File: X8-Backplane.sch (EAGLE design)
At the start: 3 parts

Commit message: Fleshing out the idea for the backplane
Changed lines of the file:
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@@
 <part name="FRAME1" library="frames" deviceset="A4-SMALL-DOCFIELD" device=""/>
 <part name="U$1" library="HSEC8-1xx-01-XX-DV-A" deviceset="HSEC8-140-01-XX-DV-A" device=""/>
+<part name="U$17" library="HSEC8-1xx-01-XX-DV-A" deviceset="HSEC8-140-01-XX-DV-A" device=""/>
 <part name="U$2" library="HSEC8-1xx-01-XX-DV-A" deviceset="HSEC8-160-01-XX-DV-A" device=""/>
-<part name="U$17" library="HSEC8-1xx-01-XX-DV-A" deviceset="HSEC8-140-01-XX-DV-A" device=""/>
 </parts>
 <sheets>
@@
 <instance part="FRAME1" gate="/1" x="0" y="0"/>
 <instance part="U$1" gate="G$1" x="50.8" y="190.5"/>
-<instance part="U$2" gate="G$1" x="114.3" y="220.98"/>
 <instance part="U$17" gate="G$1" x="15.24" y="190.5"/>
+<instance part="U$2" gate="G$1" x="91.44" y="185.42"/>
 </instances>
 <busses>

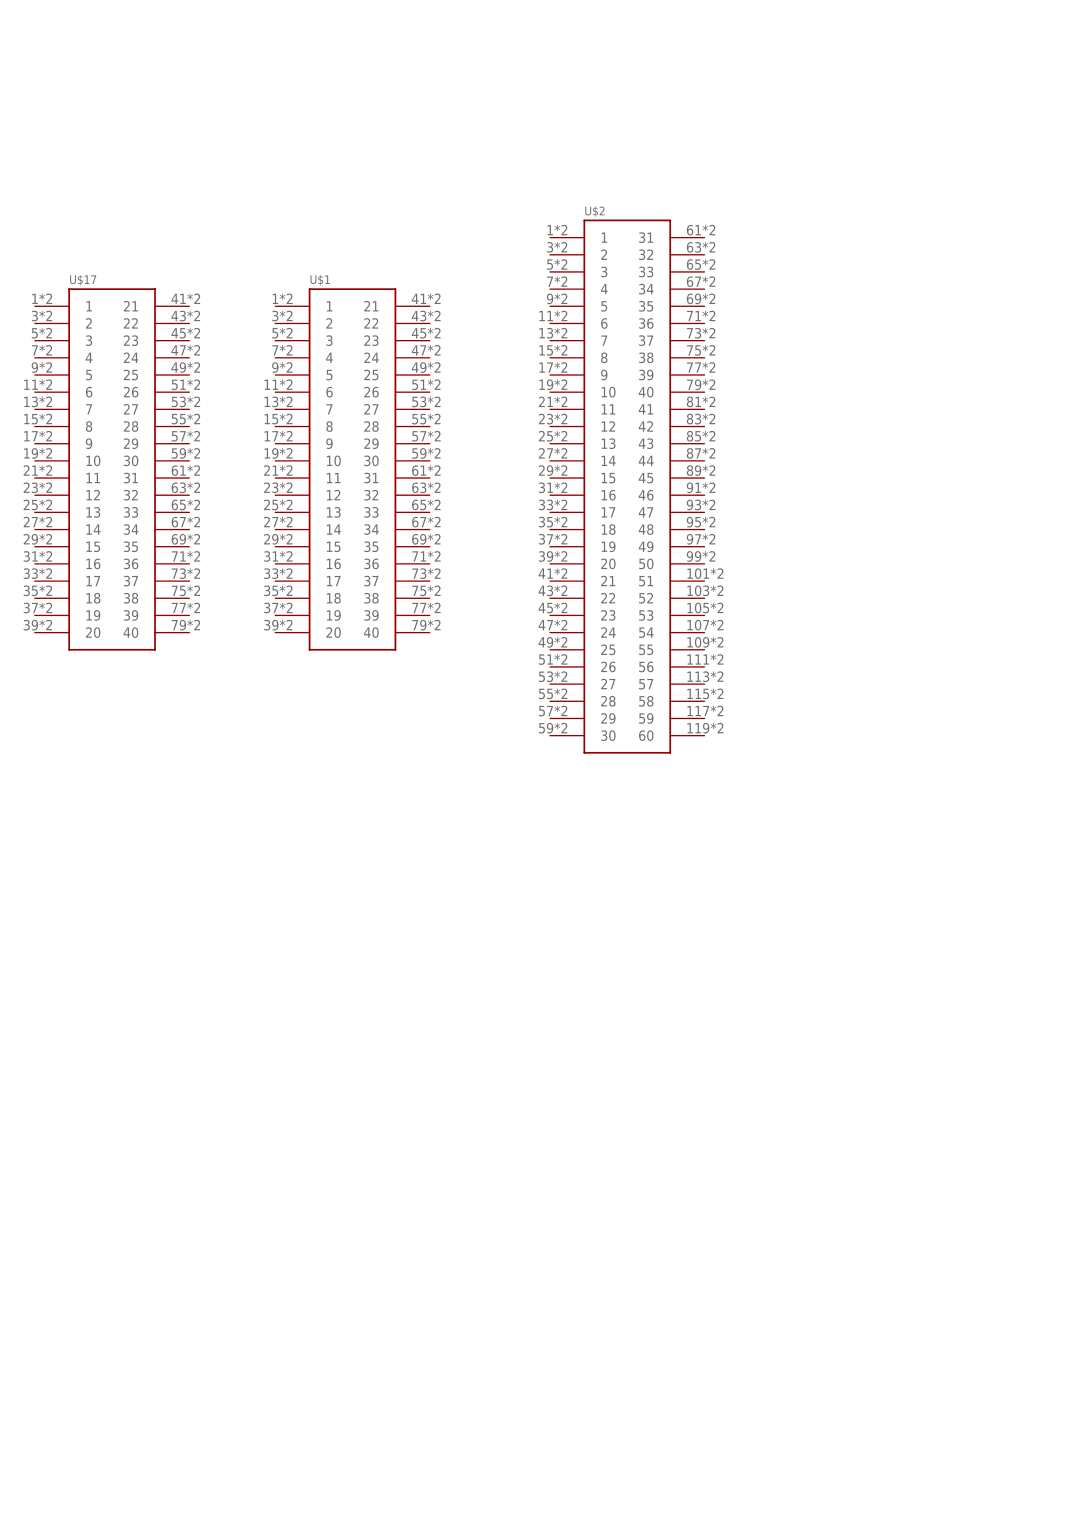
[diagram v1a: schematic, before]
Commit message: Added more connections to the backplane
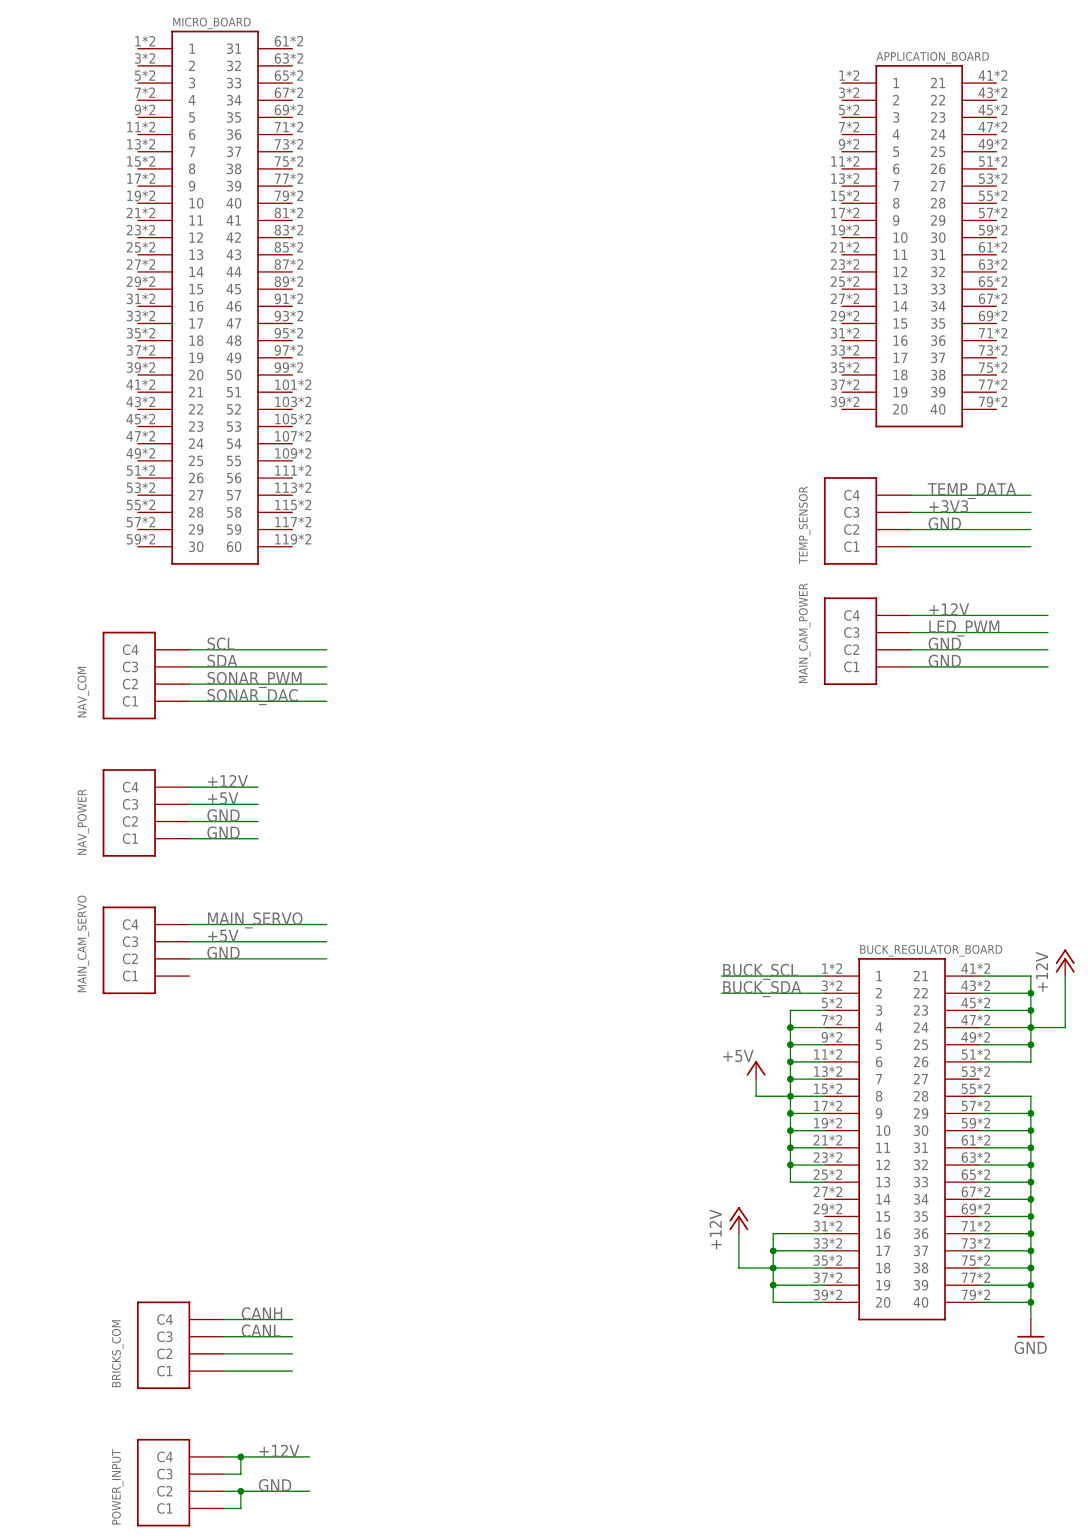
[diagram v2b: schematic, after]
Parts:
- removed U$1, U$17: HSEC8-140-01-XX-DV-A, HSEC8-1xx-01-XX-DV-A:HSEC8-140-01-XX-DV-A
- removed U$2: HSEC8-160-01-XX-DV-A, HSEC8-1xx-01-XX-DV-A:HSEC8-160-01-XX-DV-A
- added APPLICATION_BOARD, BUCK_REGULATOR_BOARD: HSEC8-140-01-XX-DV-A, HSEC8-1xx-01-XX-DV-A:HSEC8-140-01-XX-DV-A
- added BRICKS_COM, MAIN_CAM_POWER, MAIN_CAM_SERVO, NAV_COM, NAV_POWER, POWER_INPUT, TEMP_SENSOR: MICRO-FIT-4-SMD-PART, Connectors:MICRO-FIT-4-SMD-PART
- added MICRO_BOARD: HSEC8-160-01-XX-DV-A, HSEC8-1xx-01-XX-DV-A:HSEC8-160-01-XX-DV-A
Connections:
- new net +12V: BUCK_REGULATOR_BOARD.16, BUCK_REGULATOR_BOARD.17, BUCK_REGULATOR_BOARD.18, BUCK_REGULATOR_BOARD.19, BUCK_REGULATOR_BOARD.20, BUCK_REGULATOR_BOARD.21, BUCK_REGULATOR_BOARD.22, BUCK_REGULATOR_BOARD.23, BUCK_REGULATOR_BOARD.24, BUCK_REGULATOR_BOARD.25, BUCK_REGULATOR_BOARD.26, MAIN_CAM_POWER.C4, NAV_POWER.C4, POWER_INPUT.C3, POWER_INPUT.C4
- new net +3V3: TEMP_SENSOR.C3
- new net +5V: BUCK_REGULATOR_BOARD.10, BUCK_REGULATOR_BOARD.11, BUCK_REGULATOR_BOARD.12, BUCK_REGULATOR_BOARD.13, BUCK_REGULATOR_BOARD.3, BUCK_REGULATOR_BOARD.4, BUCK_REGULATOR_BOARD.5, BUCK_REGULATOR_BOARD.6, BUCK_REGULATOR_BOARD.7, BUCK_REGULATOR_BOARD.8, BUCK_REGULATOR_BOARD.9, MAIN_CAM_SERVO.C3, NAV_POWER.C3
- new net BUCK_SCL: BUCK_REGULATOR_BOARD.1
- new net BUCK_SDA: BUCK_REGULATOR_BOARD.2
- new net CANH: BRICKS_COM.C4
- new net CANL: BRICKS_COM.C3
- new net GND: BUCK_REGULATOR_BOARD.28, BUCK_REGULATOR_BOARD.29, BUCK_REGULATOR_BOARD.30, BUCK_REGULATOR_BOARD.31, BUCK_REGULATOR_BOARD.32, BUCK_REGULATOR_BOARD.33, BUCK_REGULATOR_BOARD.34, BUCK_REGULATOR_BOARD.35, BUCK_REGULATOR_BOARD.36, BUCK_REGULATOR_BOARD.37, BUCK_REGULATOR_BOARD.38, BUCK_REGULATOR_BOARD.39, BUCK_REGULATOR_BOARD.40, MAIN_CAM_POWER.C1, MAIN_CAM_POWER.C2, MAIN_CAM_SERVO.C2, NAV_POWER.C1, NAV_POWER.C2, POWER_INPUT.C1, POWER_INPUT.C2, TEMP_SENSOR.C2
- new net LED_PWM: MAIN_CAM_POWER.C3
- new net MAIN_SERVO: MAIN_CAM_SERVO.C4
- new net N$3: BRICKS_COM.C2
- new net N$5: BRICKS_COM.C1
- new net N$7: TEMP_SENSOR.C1
- new net SCL: NAV_COM.C4
- new net SDA: NAV_COM.C3
- new net SONAR_DAC: NAV_COM.C1
- new net SONAR_PWM: NAV_COM.C2
- new net TEMP_DATA: TEMP_SENSOR.C4

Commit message: Added more connectors to the backplane schematic
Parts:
- removed MAIN_CAM_POWER, MAIN_CAM_SERVO: MICRO-FIT-4-SMD-PART, Connectors:MICRO-FIT-4-SMD-PART
- added ETH_POWER, EXTRA_SERVO, MAIN_CAM_DATA, MAIN_CAM_POW, SEC_CAM_1, SEC_CAM_2, SOLENOID_DATA, SOLENOID_POWER: MICRO-FIT-4-SMD-PART, Connectors:MICRO-FIT-4-SMD-PART
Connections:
- new net CLK: SOLENOID_DATA.C3
- new net DATA: SOLENOID_DATA.C1
- new net ENABLE: SOLENOID_DATA.C2
- new net SECOND_SERVO: EXTRA_SERVO.C4
- net +12V: now also MAIN_CAM_POW.C4, SEC_CAM_1.C3, SEC_CAM_1.C4, SEC_CAM_2.C3, SEC_CAM_2.C4, SOLENOID_POWER.C3, SOLENOID_POWER.C4; no longer MAIN_CAM_POWER.C4
- net +5V: now also ETH_POWER.C3, ETH_POWER.C4, EXTRA_SERVO.C3, MAIN_CAM_POW.C2, MAIN_CAM_POW.C3, SOLENOID_DATA.C4; no longer MAIN_CAM_SERVO.C3
- net GND: now also ETH_POWER.C1, ETH_POWER.C2, EXTRA_SERVO.C2, MAIN_CAM_DATA.C1, MAIN_CAM_DATA.C2, MAIN_CAM_POW.C1, SEC_CAM_1.C1, SEC_CAM_1.C2, SEC_CAM_2.C1, SEC_CAM_2.C2, SOLENOID_POWER.C1, SOLENOID_POWER.C2; no longer MAIN_CAM_POWER.C1, MAIN_CAM_POWER.C2, MAIN_CAM_SERVO.C2
- net LED_PWM: now also MAIN_CAM_DATA.C3; no longer MAIN_CAM_POWER.C3
- net MAIN_SERVO: now also MAIN_CAM_DATA.C4; no longer MAIN_CAM_SERVO.C4
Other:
- moved on the sheet: APPLICATION_BOARD, BRICKS_COM, MICRO_BOARD, NAV_COM, NAV_POWER, POWER_INPUT, TEMP_SENSOR

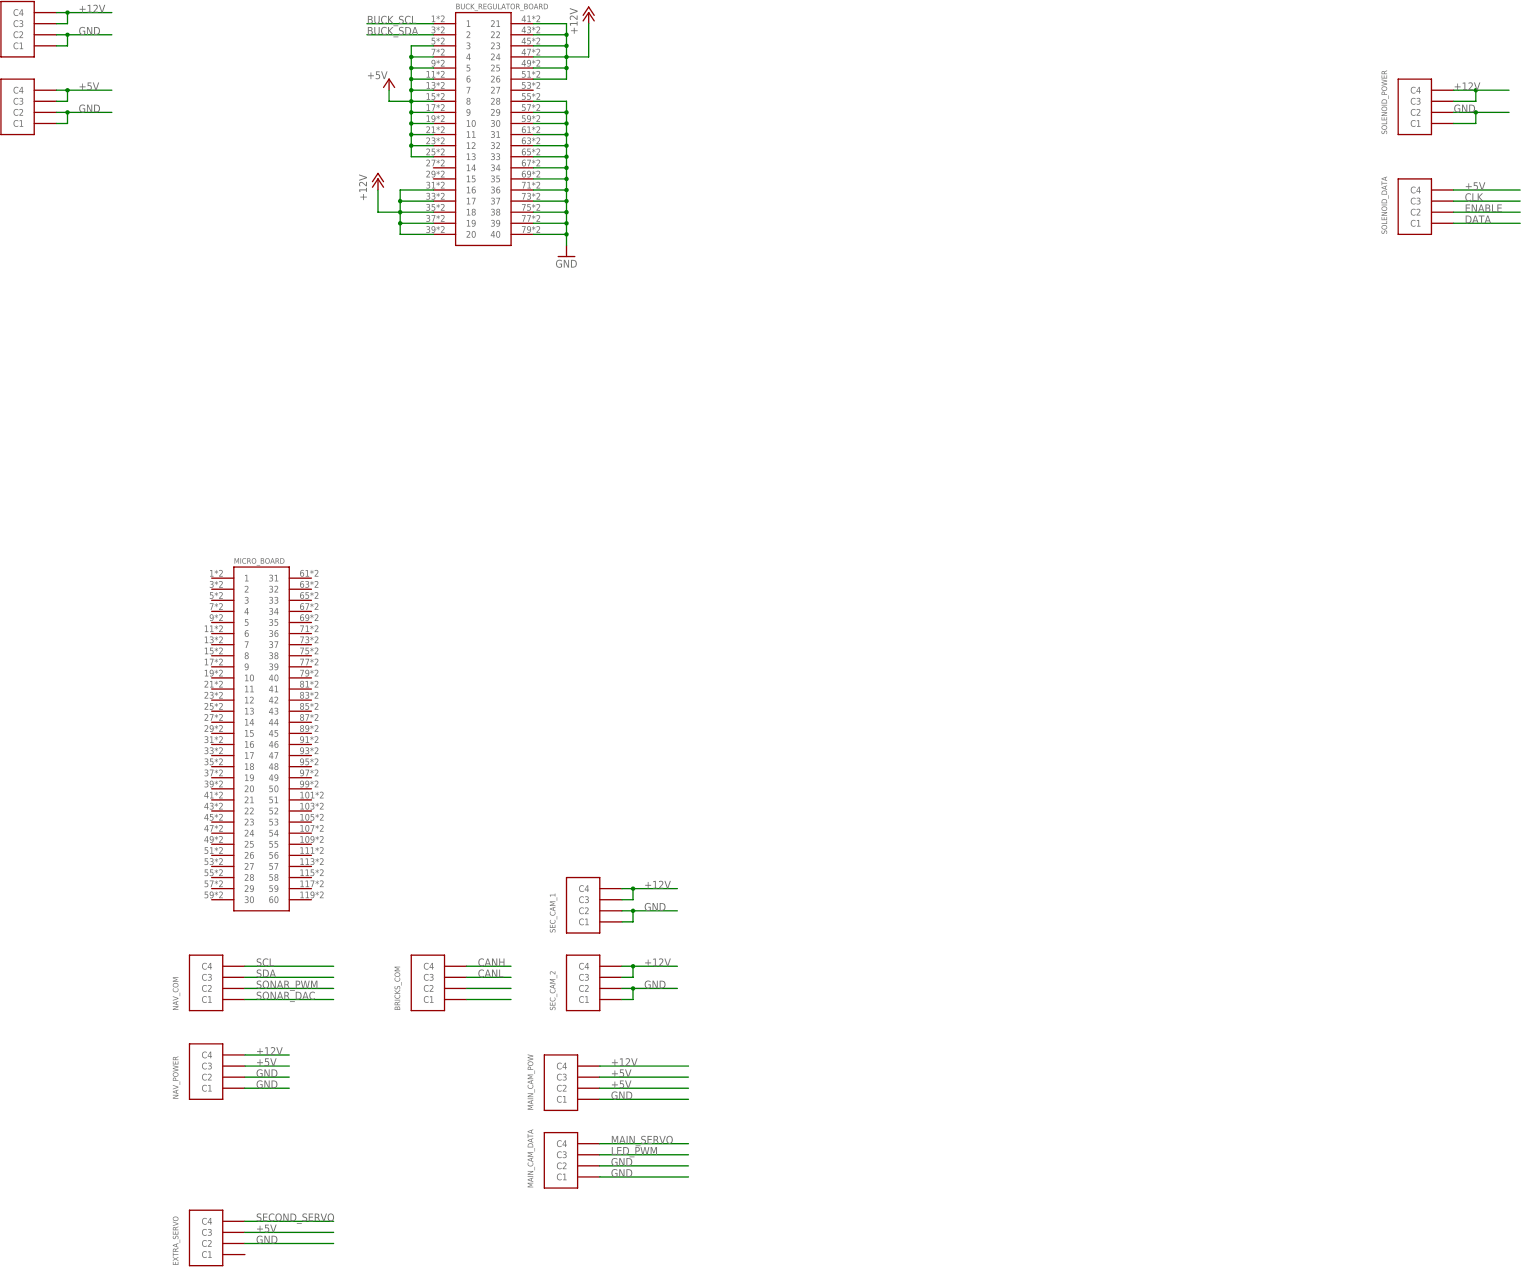
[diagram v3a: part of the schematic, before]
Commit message: First placement of parts
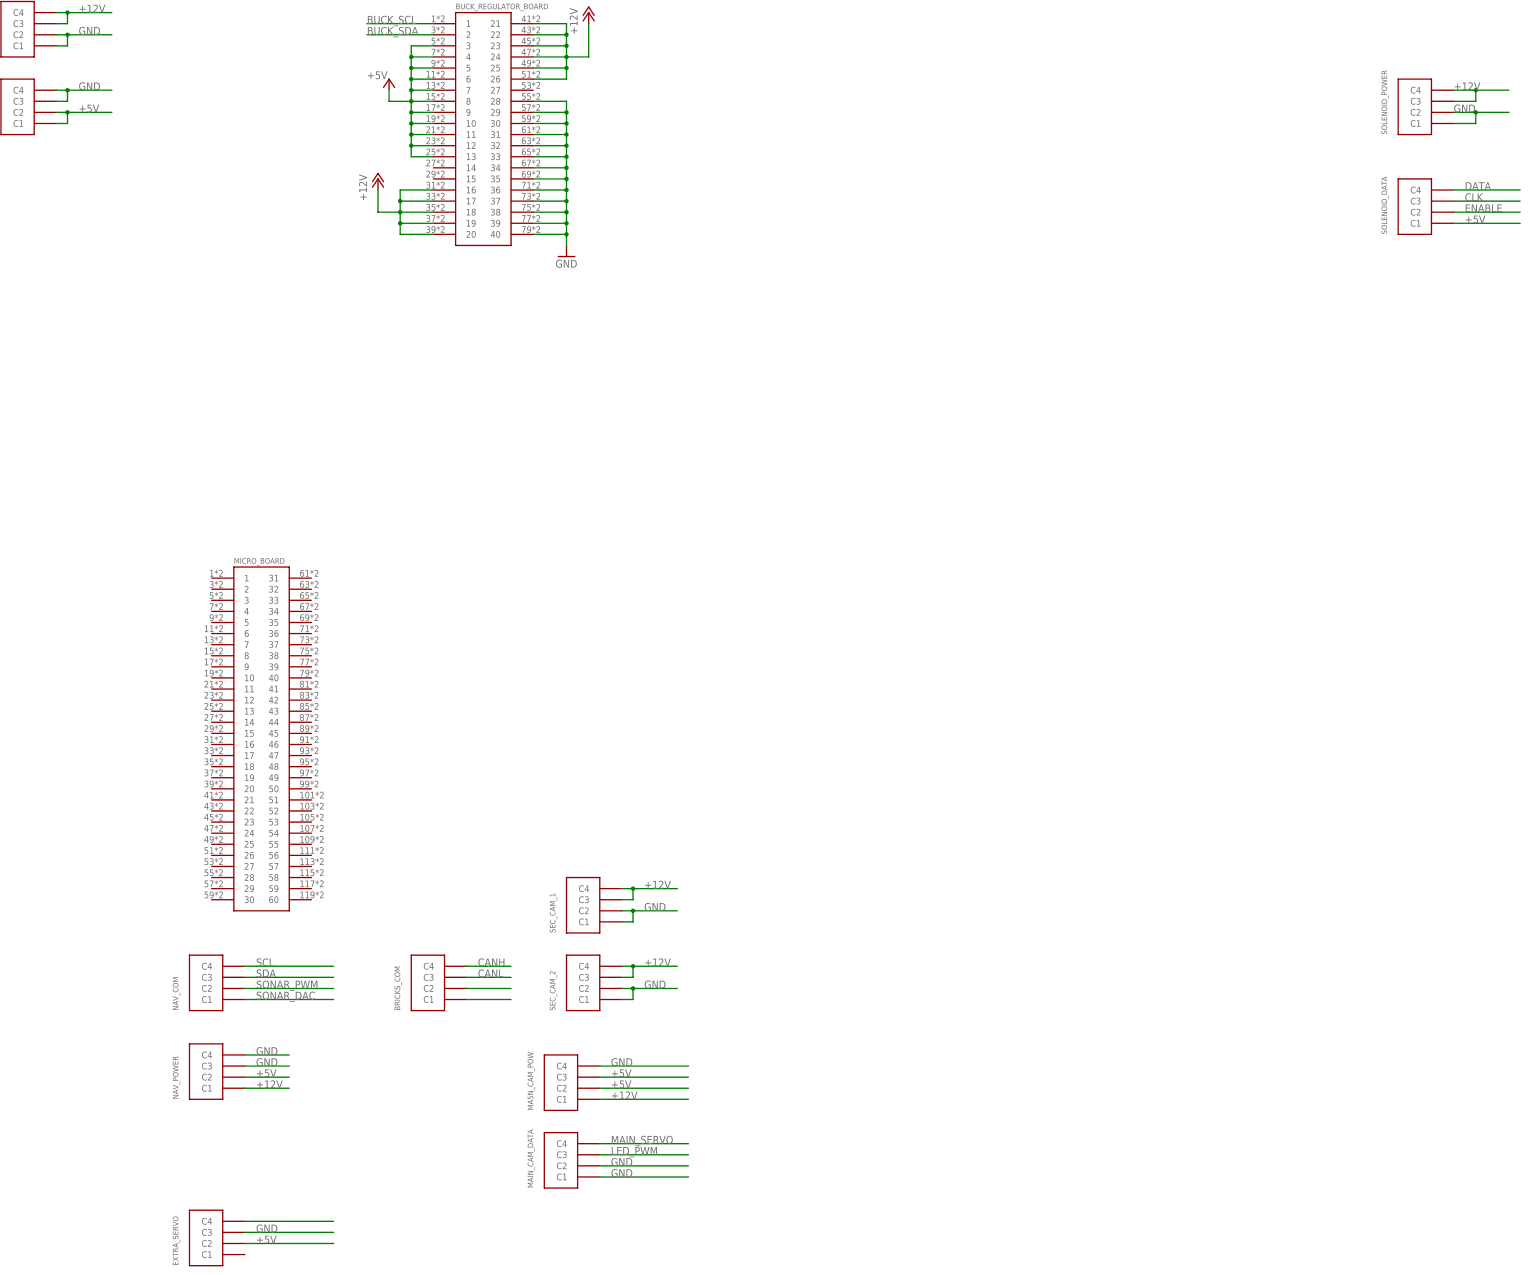
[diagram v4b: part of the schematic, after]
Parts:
- renumbered MAIN_CAM_POW to MA5N_CAM_POW
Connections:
- net +12V: now also MA5N_CAM_POW.C1, NAV_POWER.C1; no longer MA5N_CAM_POW.C4, NAV_POWER.C4
- net +5V: now also ETH_POWER.C1, ETH_POWER.C2, EXTRA_SERVO.C2, NAV_POWER.C2, SOLENOID_DATA.C1; no longer ETH_POWER.C3, ETH_POWER.C4, EXTRA_SERVO.C3, NAV_POWER.C3, SOLENOID_DATA.C4
- net DATA: now also SOLENOID_DATA.C4; no longer SOLENOID_DATA.C1
- net GND: now also ETH_POWER.C3, ETH_POWER.C4, EXTRA_SERVO.C3, MA5N_CAM_POW.C4, NAV_POWER.C3, NAV_POWER.C4; no longer ETH_POWER.C1, ETH_POWER.C2, EXTRA_SERVO.C2, MA5N_CAM_POW.C1, NAV_POWER.C1, NAV_POWER.C2
